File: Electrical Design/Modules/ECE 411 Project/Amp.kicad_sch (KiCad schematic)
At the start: 31 parts, among them J3 AudioJack3, J4 Barrel_Jack, J5 Pheonix Latching Connector (1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, U9 TPA3136D2PWPR

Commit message: kicad business
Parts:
- removed J5: Pheonix Latching Connector (1190297), Pheonix-2P-Level1190297:PHOENIX_1190297, symbol Pheonix-1190297:1190297
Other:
- note added: "Mono Summing Input (JACK FOR TESTING ONLY)"
- note added: "NOTE: THIS SHEET IS COPIED FROM DEV BOARD DESIGN. IT WILL BE UPDATED LATER ONCE THE DESIGN IS CONFIRMED TO BE FUNCTIONAL."
- note added: "PRELIMINARY"
- note added: "Power Input (JACK FOR TESTING ONLY)"
- note removed: "Mono Summing Input"
- note removed: "Output to 8ohm speaker"
- note removed: "Power Input"
- company: (none) -> Portland State University
- title: (none) -> 20W Mono Class-D Audio Amplifier
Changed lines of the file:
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@@
 	(generator_version "8.0")
 	(paper "A4")
+	(title_block
+		(title "20W Mono Class-D Audio Amplifier")
+		(rev "2.3")
+		(company "Portland State University")
+		(comment 1 "Open Source Hardware")
+		(comment 2 "Design: Eric Sanman")
+	)
 	(junction
 		(at 93.98 64.77)
@@
 	)
 	(junction
-		(at 220.345 91.44)
-		(diameter 0)
-		(color 0 0 0 0)
-	)
-	(junction
 		(at 123.825 74.93)
 		(diameter 0)
@@
 	)
 	(junction
-		(at 220.345 99.06)
-		(diameter 0)
-		(color 0 0 0 0)
-	)
-	(junction
 		(at 125.095 130.81)
 		(diameter 0)
@@
 	(wire
 		(pts
-			(xy 220.345 91.44) (xy 220.345 93.98)
-		)
-		(stroke
-			(width 0)
-			(type default)
-		)
-	)
-	(wire
-		(pts
 			(xy 65.405 80.645) (xy 65.405 83.185)
 		)
@@
 	(wire
 		(pts
+			(xy 220.345 93.98) (xy 222.885 93.98)
+		)
+		(stroke
+			(width 0)
+			(type default)
+		)
+	)
+	(wire
+		(pts
 			(xy 197.485 86.36) (xy 206.375 86.36)
 		)
@@
 	(wire
 		(pts
-			(xy 220.345 96.52) (xy 220.345 99.06)
+			(xy 220.345 96.52) (xy 220.345 105.41)
 		)
 		(stroke
@@
 	(wire
 		(pts
-			(xy 220.345 99.06) (xy 220.345 105.41)
-		)
-		(stroke
-			(width 0)
-			(type default)
-		)
-	)
-	(wire
-		(pts
 			(xy 179.07 99.06) (xy 180.975 99.06)
 		)
@@
 	(wire
 		(pts
-			(xy 220.345 86.36) (xy 220.345 91.44)
+			(xy 220.345 86.36) (xy 220.345 93.98)
 		)
 		(stroke
@@
 	(wire
 		(pts
+			(xy 220.345 96.52) (xy 222.885 96.52)
+		)
+		(stroke
+			(width 0)
+			(type default)
+		)
+	)
+	(wire
+		(pts
 			(xy 169.545 99.06) (xy 169.545 101.6)
 		)
@@
 		)
 	)
+	(rectangle
+		(start 223.52 153.035)
+		(end 282.575 163.195)
+		(stroke
+			(width 1.27)
+			(type default)
+			(color 194 0 0 1)
+		)
+		(fill
+			(type none)
+		)
+	)
 	(image
 		(at 271.78 174.625)
@@
 		)
 	)
-	(text "Mono Summing Input"
+	(text "Mono Summing Input (JACK FOR TESTING ONLY)"
 		(exclude_from_sim no)
 		(at 62.23 21.59 0)
@@
 		)
 	)
-	(text "Power Input"
+	(text "PRELIMINARY"
+		(exclude_from_sim no)
+		(at 252.73 160.655 0)
+		(effects
+			(font
+				(face "Arial Black")
+				(size 5.08 5.08)
+				(thickness 0.762)
+				(bold yes)
+				(color 194 0 0 1)
+			)
+		)
+	)
+	(text "NOTE: \nTHIS SHEET IS COPIED FROM DEV BOARD DESIGN.\nIT WILL BE UPDATED LATER ONCE THE DESIGN IS CONFIRMED\nTO BE FUNCTIONAL."
+		(exclude_from_sim no)
+		(at 20.32 182.245 0)
+		(effects
+			(font
+				(size 2.54 2.54)
+				(thickness 0.508)
+				(bold yes)
+				(color 194 0 0 1)
+			)
+			(justify left)
+		)
+	)
+	(text "Power Input (JACK FOR TESTING ONLY)"
 		(exclude_from_sim no)
 		(at 111.125 21.59 0)
@@
 		)
 	)
-	(text "Output to 8ohm speaker"
-		(exclude_from_sim no)
-		(at 234.569 97.028 0)
-		(effects
-			(font
-				(size 1.27 1.27)
-			)
-			(justify left bottom)
-		)
-	)
 	(text "4.5-14 V DC"
 		(exclude_from_sim no)
@@
 		)
 	)
+	(hierarchical_label "SPK-"
+		(shape output)
+		(at 222.885 96.52 0)
+		(fields_autoplaced yes)
+		(effects
+			(font
+				(size 1.27 1.27)
+			)
+			(justify left)
+		)
+	)
+	(hierarchical_label "SPK+"
+		(shape output)
+		(at 222.885 93.98 0)
+		(fields_autoplaced yes)
+		(effects
+			(font
+				(size 1.27 1.27)
+			)
+			(justify left)
+		)
+	)
 	(symbol
 		(lib_name "GND_2")
@@
 					(unit 1)
 				)
-			)
-		)
-	)
-	(symbol
-		(lib_id "Pheonix-1190297:1190297")
-		(at 227.965 93.98 0)
-		(mirror x)
-		(unit 1)
-		(exclude_from_sim no)
-		(in_bom yes)
-		(on_board yes)
-		(dnp no)
-		(property "Reference" "J5"
-			(at 234.315 96.5201 0)
-			(effects
-				(font
-					(size 1.27 1.27)
-				)
-				(justify left)
-			)
-		)
-		(property "Value" "Pheonix Latching Connector (1190297)"
-			(at 234.315 93.98 0)
-			(effects
-				(font
-					(size 1 1)
-				)
-				(justify left)
-			)
-		)
-		(property "Footprint" "Pheonix-2P-Level1190297:PHOENIX_1190297"
-			(at 227.965 93.98 0)
-			(effects
-				(font
-					(size 1.27 1.27)
-				)
-				(justify bottom)
-				(hide yes)
-			)
-		)
-		(property "Datasheet" "http://www.neutrik.com/en/speakon/"
-			(at 227.965 93.98 0)
-			(effects
-				(font
-					(size 1.27 1.27)
-				)
-				(hide yes)
-			)
-		)
-		(property "Description" ""
-			(at 227.965 93.98 0)
-			(effects
-				(font
-					(size 1.27 1.27)
-				)
-				(hide yes)
-			)
-		)
-		(property "PARTREV" "03.11.2020"
-			(at 227.965 93.98 0)
-			(effects
-				(font
-					(size 1.27 1.27)
-				)
-				(justify bottom)
-				(hide yes)
-			)
-		)
-		(property "STANDARD" "Manufacturer Recommendations"
-			(at 227.965 93.98 0)
-			(effects
-				(font
-					(size 1.27 1.27)
-				)
-				(justify bottom)
-				(hide yes)
-			)
-		)
-		(property "MAXIMUM_PACKAGE_HEIGHT" "23.58mm"
-			(at 227.965 93.98 0)
-			(effects
-				(font
-					(size 1.27 1.27)
-				)
-				(justify bottom)
-				(hide yes)
-			)
-		)
-		(property "MANUFACTURER" "Phoenix Contact"
-			(at 227.965 93.98 0)
-			(effects
-				(font
-					(size 1.27 1.27)
-				)
-				(justify bottom)
-				(hide yes)
-			)
-		)
-		(pin "2_2"
-		)
-		(pin "1_2"
-		)
-		(pin "1_1"
-		)
-		(pin "2_1"
-		)
-		(instances
-			(project "ECE 411 Project"
-				(path "/2625e5a1-d0c8-41ce-941d-75d035a5f1c5/fc48e9dd-306b-4a9b-831b-312573108cdc"
-					(reference "J5")
-					(unit 1)
-				)

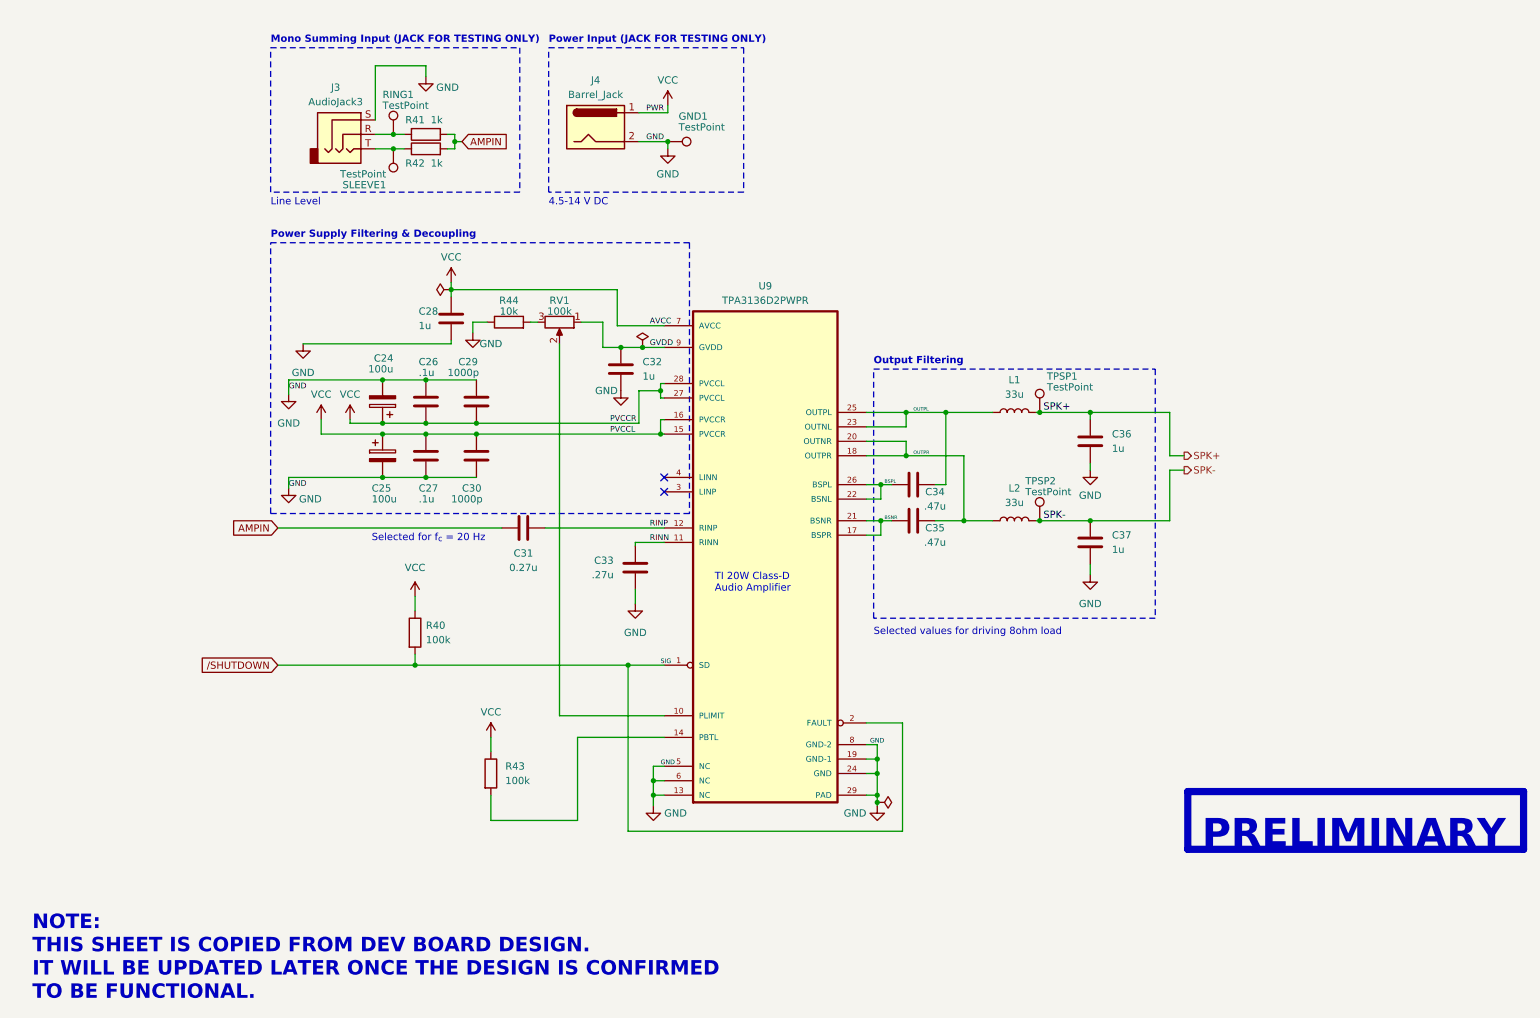
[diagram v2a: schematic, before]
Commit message: schematic, start layout
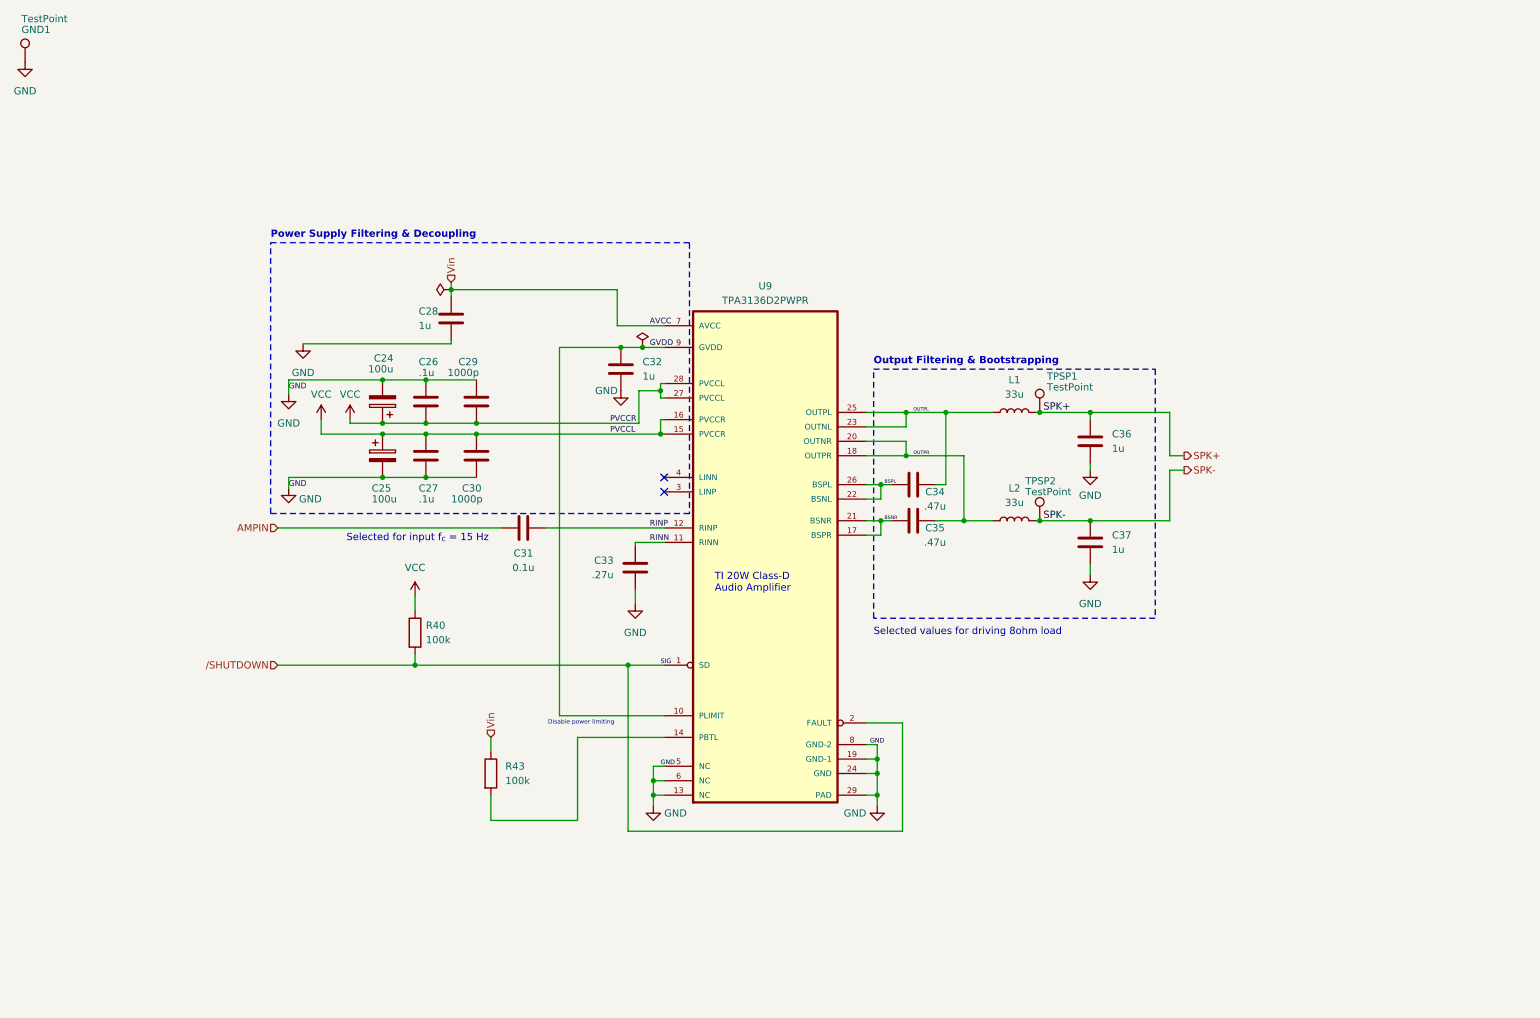
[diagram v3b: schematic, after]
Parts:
- removed J3: AudioJack3, Connector_Audio:Jack_3.5mm_CUI_SJ-3523-SMT_Horizontal, symbol Connector_Audio:AudioJack3
- removed J4: Barrel_Jack, Connector_BarrelJack:BarrelJack_Wuerth_6941xx301002, symbol Connector:Barrel_Jack
- removed R41, R42: 1k, Resistor_SMD:R_0402_1005Metric_Pad0.72x0.64mm_HandSolder, symbol Device:R
- removed R44: 10k, Resistor_SMD:R_0402_1005Metric_Pad0.72x0.64mm_HandSolder, symbol Device:R
- removed RING1, SLEEVE1: TestPoint, TestPoint:TestPoint_Bridge_Pitch2.0mm_Drill0.7mm, symbol Connector:TestPoint
- removed RV1: 100k, Potentiometer_THT:Potentiometer_Bourns_3386P_Vertical, symbol Device:R_Potentiometer
- C31: value 0.27u -> 0.1u
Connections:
- net GVDD: now also U9.10 (PLIMIT)
- net VCC: no longer C28.1, R43.1, U9.7 (AVCC)
- new net Vin: C28.1, R43.1, U9.7 (AVCC)
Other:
- note added: "Disable power limiting"
- note added: "Output Filtering & Bootstrapping"
- note added: "Selected for input f_{c} = 15 Hz"
- note removed: "4.5-14 V DC"
- note removed: "Line Level"
- note removed: "Mono Summing Input (JACK FOR TESTING ONLY)"
- note removed: "NOTE: THIS SHEET IS COPIED FROM DEV BOARD DESIGN. IT WILL BE UPDATED LATER ONCE THE DESIGN IS CONFIRMED TO BE FUNCTIONAL."
- note removed: "Output Filtering"
- note removed: "PRELIMINARY"
- note removed: "Power Input (JACK FOR TESTING ONLY)"
- note removed: "Selected for f_{c} = 20 Hz"
- moved on the sheet: GND1

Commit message: update BOM
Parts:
- C24, C25, C26, C27, C28, C32, C36, C37, GND1, TPSP1, TPSP2: Part Origin (none) -> DK
- C29, C30, C31, C33: footprint Capacitor_SMD:C_0402_1005Metric_Pad0.74x0.62mm_HandSolder -> Capacitor_SMD:C_0805_2012Metric_Pad1.18x1.45mm_HandSolder; Part Origin (none) -> DK
- C34, C35: footprint Capacitor_SMD:C_0402_1005Metric_Pad0.74x0.62mm_HandSolder -> Capacitor_SMD:C_0805_2012Metric_Pad1.18x1.45mm_HandSolder; On Hand (On Way) (none) -> (100); Part Number (none) -> 1276-1074-1-ND; Part Origin (none) -> DK
- R40, R43: footprint Resistor_SMD:R_0402_1005Metric_Pad0.72x0.64mm_HandSolder -> Resistor_SMD:R_0805_2012Metric_Pad1.20x1.40mm_HandSolder; Part Origin (none) -> DK
- U9: Part Origin (none) -> SBP
